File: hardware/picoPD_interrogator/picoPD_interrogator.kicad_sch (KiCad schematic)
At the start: 29 parts, among them Q1 rohm-RE1C002UN, Q2 rohm-RE1C002UN, Q3 rohm-RE1C002UN, Q4 rohm-RE1C002UN, U2 ST-LM393QT

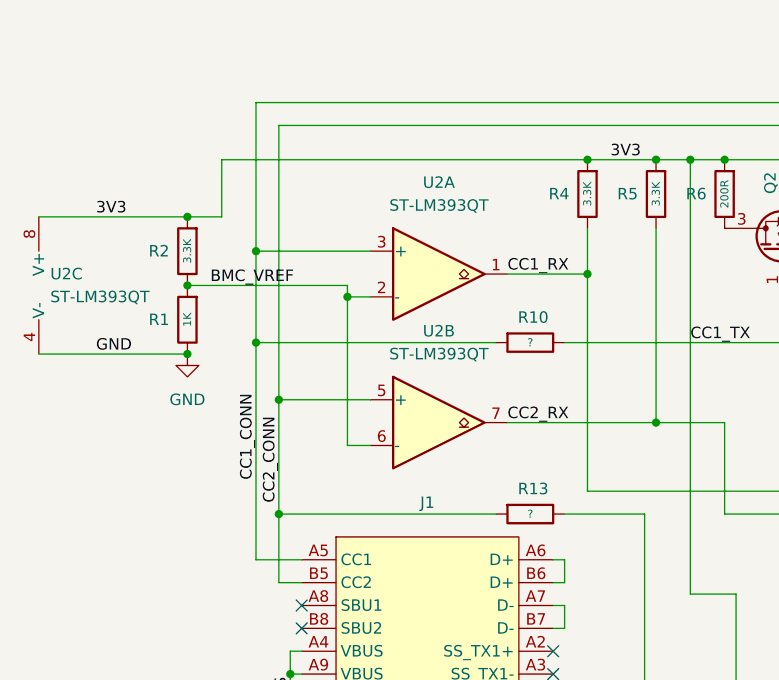
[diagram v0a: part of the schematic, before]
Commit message: Schematic - swapped comparator + and - inputs.
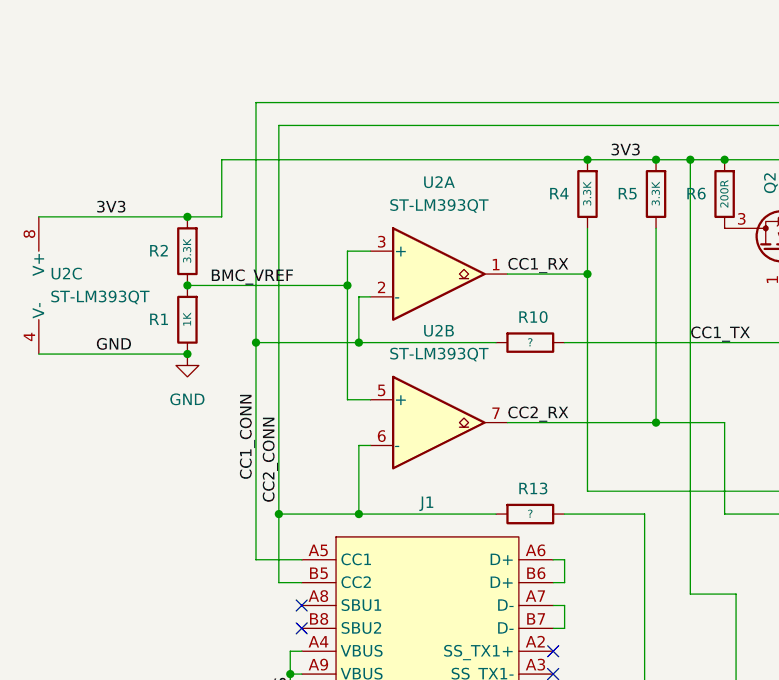
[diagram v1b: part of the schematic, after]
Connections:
- net BMC_VREF: now also U2.3 (+), U2.5 (+); no longer U2.2 (-), U2.6 (-)
- net CC1_CONN: now also U2.2 (-); no longer U2.3 (+)
- net CC2_CONN: now also U2.6 (-); no longer U2.5 (+)
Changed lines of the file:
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@@
+	)
+	(junction
+		(at 74.93 110.49)
+		(diameter 0)
+		(color 0 0 0 0)
+	)
+	(junction
+		(at 74.93 102.87)
+		(diameter 0)
+		(color 0 0 0 0)
+	)
+	(junction
+		(at 220.98 52.07)
+		(diameter 0)
+		(color 0 0 0 0)
+	)
+	(junction
+		(at 115.57 35.56)
+		(diameter 0)
+		(color 0 0 0 0)
+	)
+	(junction
+		(at 73.66 74.93)
+		(diameter 0)
+		(color 0 0 0 0)
+	)
+	(junction
+		(at 135.89 45.72)
+		(diameter 0)
+		(color 0 0 0 0)
+	)
+	(junction
+		(at 170.18 69.85)
+		(diameter 0)
+		(color 0 0 0 0)
 	)
 	(junction
@@
 	)
 	(junction
-		(at 74.93 110.49)
-		(diameter 0)
-		(color 0 0 0 0)
-	)
-	(junction
-		(at 74.93 102.87)
-		(diameter 0)
-		(color 0 0 0 0)
-	)
-	(junction
-		(at 220.98 52.07)
-		(diameter 0)
-		(color 0 0 0 0)
-	)
-	(junction
-		(at 115.57 35.56)
-		(diameter 0)
-		(color 0 0 0 0)
-	)
-	(junction
-		(at 73.66 74.93)
-		(diameter 0)
-		(color 0 0 0 0)
-	)
-	(junction
-		(at 135.89 45.72)
-		(diameter 0)
-		(color 0 0 0 0)
-	)
-	(junction
-		(at 170.18 69.85)
-		(diameter 0)
-		(color 0 0 0 0)
-	)
-	(junction
 		(at 231.14 100.33)
 		(diameter 0)
@@
 	)
 	(junction
-		(at 81.28 50.8)
-		(diameter 0)
-		(color 0 0 0 0)
-	)
-	(junction
 		(at 205.74 69.85)
 		(diameter 0)
@@
 	)
 	(junction
+		(at 81.28 49.53)
+		(diameter 0)
+		(color 0 0 0 0)
+	)
+	(junction
 		(at 205.74 95.25)
 		(diameter 0)
@@
 	)
 	(junction
+		(at 82.55 55.88)
+		(diameter 0)
+		(color 0 0 0 0)
+	)
+	(junction
 		(at 205.74 107.95)
 		(diameter 0)
@@
 	)
 	(junction
-		(at 71.12 45.72)
+		(at 82.55 74.93)
 		(diameter 0)
 		(color 0 0 0 0)
@@
 	)
 	(junction
-		(at 73.66 62.23)
-		(diameter 0)
-		(color 0 0 0 0)
-	)
-	(junction
 		(at 71.12 55.88)
 		(diameter 0)
@@
 	(wire
 		(pts
-			(xy 73.66 62.23) (xy 83.82 62.23)
-		)
-		(stroke
-			(width 0)
-			(type default)
-		)
-	)
-	(wire
-		(pts
 			(xy 170.18 57.15) (xy 172.72 57.15)
 		)
@@
 	(wire
 		(pts
+			(xy 82.55 55.88) (xy 71.12 55.88)
+		)
+		(stroke
+			(width 0)
+			(type default)
+		)
+	)
+	(wire
+		(pts
 			(xy 74.93 92.71) (xy 74.93 90.17)
 		)
@@
 	(wire
 		(pts
-			(xy 97.79 55.88) (xy 71.12 55.88)
+			(xy 97.79 55.88) (xy 82.55 55.88)
 		)
 		(stroke
@@
 	(wire
 		(pts
+			(xy 81.28 62.23) (xy 83.82 62.23)
+		)
+		(stroke
+			(width 0)
+			(type default)
+		)
+	)
+	(wire
+		(pts
 			(xy 123.19 35.56) (xy 208.28 35.56)
 		)
@@
 	(wire
 		(pts
+			(xy 71.12 29.21) (xy 71.12 55.88)
+		)
+		(stroke
+			(width 0)
+			(type default)
+		)
+	)
+	(wire
+		(pts
 			(xy 157.48 140.97) (xy 143.51 140.97)
 		)
@@
 	(wire
 		(pts
-			(xy 81.28 50.8) (xy 83.82 50.8)
-		)
-		(stroke
-			(width 0)
-			(type default)
-		)
-	)
-	(wire
-		(pts
 			(xy 105.41 85.09) (xy 105.41 87.63)
 		)
@@
 	(wire
 		(pts
-			(xy 71.12 29.21) (xy 71.12 45.72)
-		)
-		(stroke
-			(width 0)
-			(type default)
-		)
-	)
-	(wire
-		(pts
 			(xy 187.96 107.95) (xy 187.96 105.41)
 		)
@@
 	(wire
 		(pts
-			(xy 71.12 45.72) (xy 71.12 55.88)
-		)
-		(stroke
-			(width 0)
-			(type default)
-		)
-	)
-	(wire
-		(pts
 			(xy 143.51 140.97) (xy 143.51 116.84)
 		)
@@
 	(wire
 		(pts
-			(xy 73.66 74.93) (xy 73.66 62.23)
+			(xy 82.55 50.8) (xy 82.55 55.88)
 		)
 		(stroke
@@
 	(wire
 		(pts
+			(xy 81.28 49.53) (xy 81.28 45.72)
+		)
+		(stroke
+			(width 0)
+			(type default)
+		)
+	)
+	(wire
+		(pts
 			(xy 105.41 55.88) (xy 133.35 55.88)
 		)
@@
 	(wire
 		(pts
-			(xy 73.66 74.93) (xy 97.79 74.93)
+			(xy 73.66 74.93) (xy 82.55 74.93)
 		)
 		(stroke
@@
 	(wire
 		(pts
+			(xy 83.82 50.8) (xy 82.55 50.8)
+		)
+		(stroke
+			(width 0)
+			(type default)
+		)
+	)
+	(wire
+		(pts
 			(xy 74.93 97.79) (xy 74.93 95.25)
 		)
@@
 	(wire
 		(pts
+			(xy 73.66 31.75) (xy 73.66 74.93)
+		)
+		(stroke
+			(width 0)
+			(type default)
+		)
+	)
+	(wire
+		(pts
 			(xy 168.91 41.91) (xy 218.44 41.91)
 		)
@@
 	(wire
 		(pts
-			(xy 81.28 50.8) (xy 81.28 49.53)
-		)
-		(stroke
-			(width 0)
-			(type default)
-		)
-	)
-	(wire
-		(pts
 			(xy 170.18 82.55) (xy 170.18 69.85)
 		)
@@
 	(wire
 		(pts
-			(xy 83.82 67.31) (xy 81.28 67.31)
-		)
-		(stroke
-			(width 0)
-			(type default)
-		)
-	)
-	(wire
-		(pts
-			(xy 71.12 45.72) (xy 83.82 45.72)
-		)
-		(stroke
-			(width 0)
-			(type default)
-		)
-	)
-	(wire
-		(pts
 			(xy 105.41 87.63) (xy 104.14 87.63)
 		)
@@
 	(wire
 		(pts
+			(xy 81.28 45.72) (xy 83.82 45.72)
+		)
+		(stroke
+			(width 0)
+			(type default)
+		)
+	)
+	(wire
+		(pts
+			(xy 82.55 74.93) (xy 97.79 74.93)
+		)
+		(stroke
+			(width 0)
+			(type default)
+		)
+	)
+	(wire
+		(pts
 			(xy 142.24 85.09) (xy 172.72 85.09)
 		)
@@
 	(wire
 		(pts
+			(xy 63.5 49.53) (xy 81.28 49.53)
+		)
+		(stroke
+			(width 0)
+			(type default)
+		)
+	)
+	(wire
+		(pts
+			(xy 82.55 67.31) (xy 82.55 74.93)
+		)
+		(stroke
+			(width 0)
+			(type default)
+		)
+	)
+	(wire
+		(pts
 			(xy 170.18 82.55) (xy 172.72 82.55)
 		)
@@
 	(wire
 		(pts
-			(xy 81.28 67.31) (xy 81.28 50.8)
-		)
-		(stroke
-			(width 0)
-			(type default)
-		)
-	)
-	(wire
-		(pts
 			(xy 99.06 64.77) (xy 115.57 64.77)
 		)
@@
 	(wire
 		(pts
-			(xy 73.66 62.23) (xy 73.66 31.75)
-		)
-		(stroke
-			(width 0)
-			(type default)
-		)
-	)
-	(wire
-		(pts
 			(xy 190.5 118.11) (xy 190.5 105.41)
 		)
@@
 	(wire
 		(pts
-			(xy 63.5 49.53) (xy 81.28 49.53)
-		)
-		(stroke
-			(width 0)
-			(type default)
-		)
-	)
-	(wire
-		(pts
 			(xy 203.2 62.23) (xy 208.28 62.23)
 		)
@@
 		)
 		(stroke
+			(width 0)
+			(type default)
+		)
+	)
+	(wire
+		(pts
+			(xy 81.28 49.53) (xy 81.28 62.23)
+		)
+		(stroke
+			(width 0)
+			(type default)
+		)
+	)
+	(wire
+		(pts
+			(xy 82.55 67.31) (xy 83.82 67.31)
+		)
+		(stroke

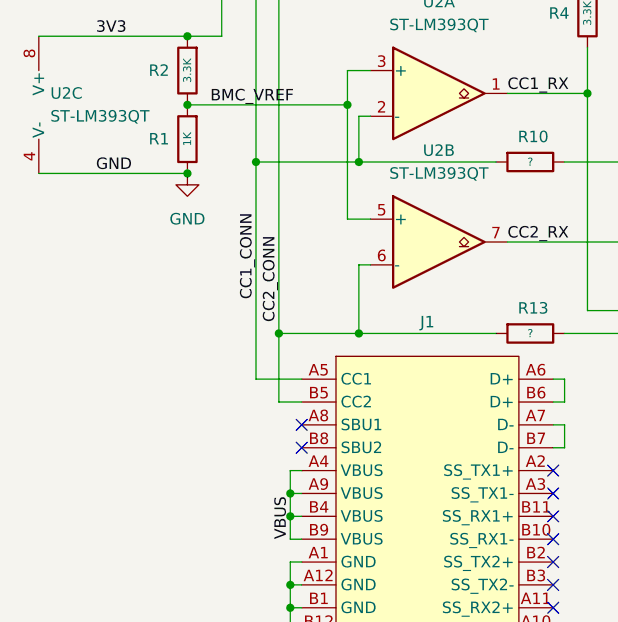
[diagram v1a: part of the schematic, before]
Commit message: Schematic - Added Rd pulldown resistors.
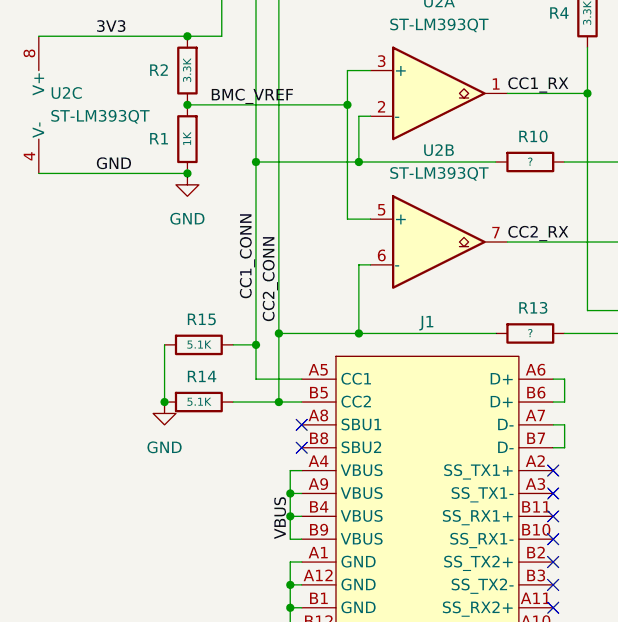
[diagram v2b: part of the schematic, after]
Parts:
- added R14, R15: 5.1K, Resistor_SMD:R_0201_0603Metric, symbol Device:R
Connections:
- net CC1_CONN: now also R15.1
- net CC2_CONN: now also R14.1
- net GND: now also R14.2, R15.2

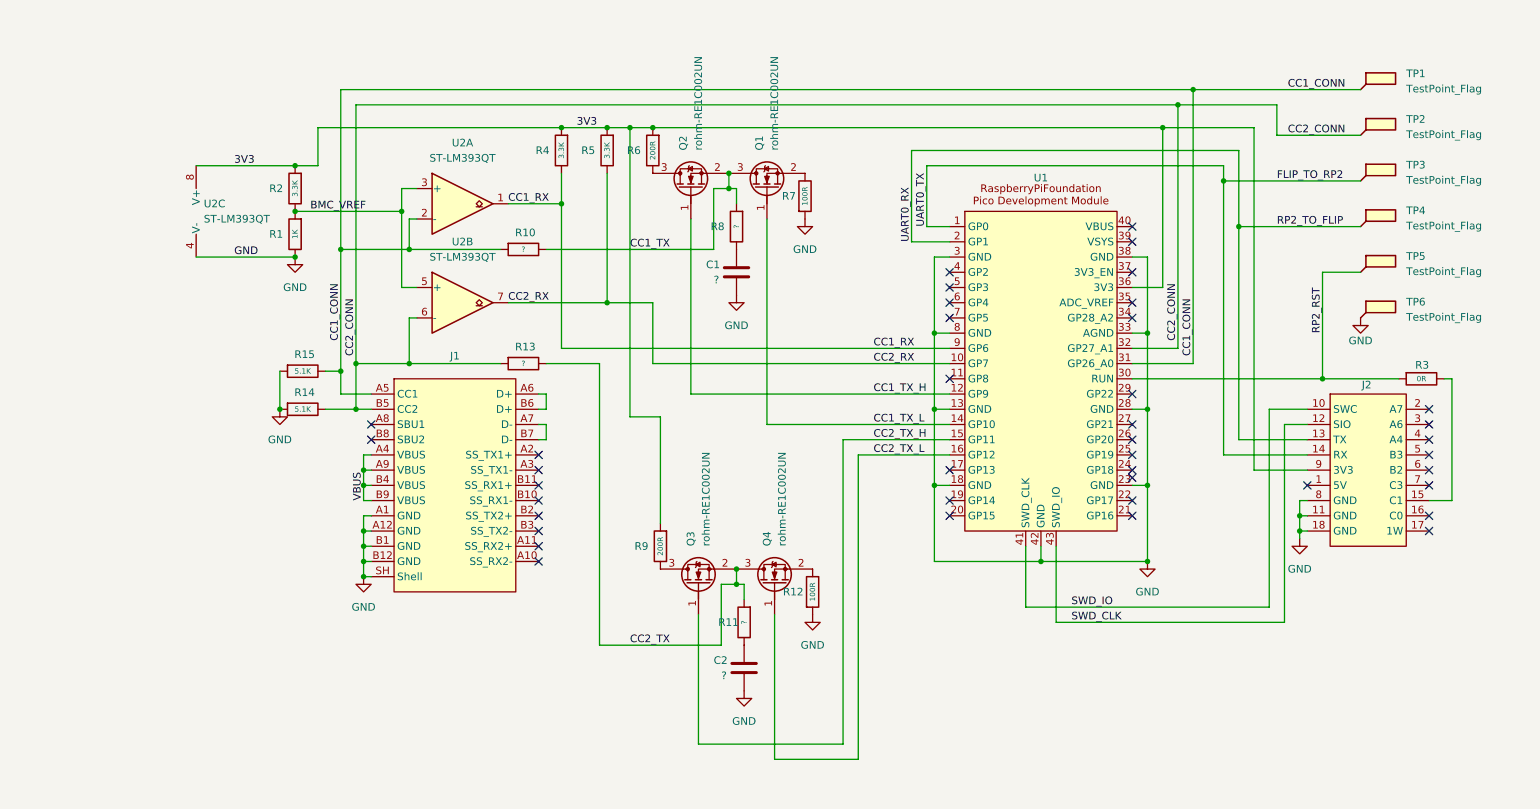
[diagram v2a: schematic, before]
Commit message: Seperated out RPI Pico MCU module on schematic.
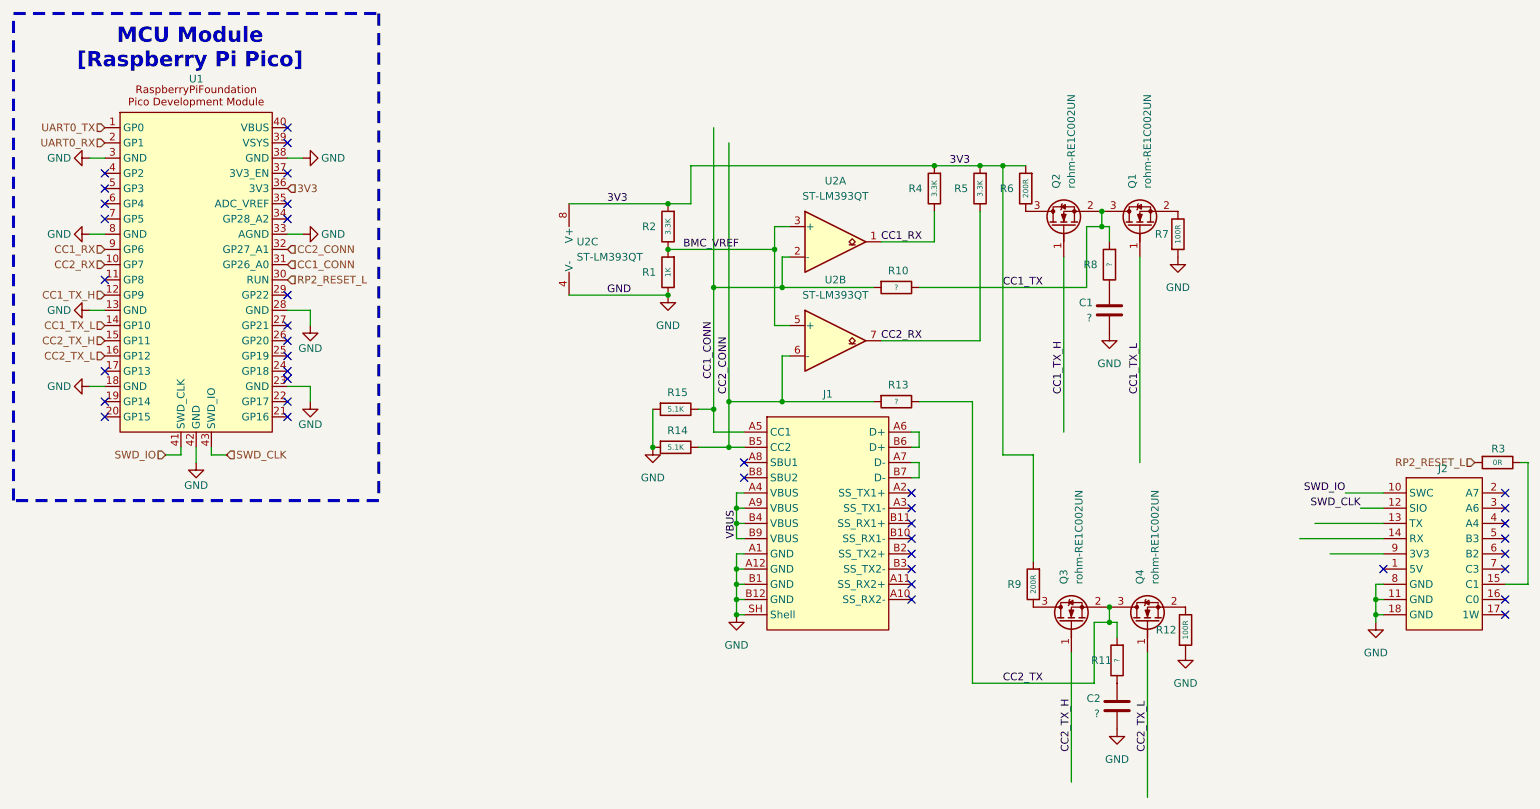
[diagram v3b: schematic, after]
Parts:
- removed TP1, TP2, TP3, TP4, TP5, TP6: TestPoint_Flag, picoPD_interrogator:Harwin_S2751, symbol Connector:TestPoint_Flag
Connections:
- net 3V3: no longer J2.9 (3V3)
- net FLIP_TO_RP2: no longer names the net of J2.14 (RX)
- net FLIP_TO_RP2: no longer U1.1 (GP0)
- net RP2_RST renamed RP2_RESET_L
- net RP2_TO_FLIP: no longer names the net of J2.13 (TX)
- net RP2_TO_FLIP: no longer U1.2 (GP1)
- new net UART0_RX: U1.2 (GP1)
- new net UART0_TX: U1.1 (GP0)
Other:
- note added: "MCU Module [Raspberry Pi Pico]"
- moved on the sheet: C1, C2, J1, J2, Q1, Q2, Q3, Q4, R1, R10, R11, R12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

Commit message: Cleaned up schematic layout.
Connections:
- net 3V3: now also J2.9 (3V3), R4.1; no longer Q1.3 (D), Q2.2 (S), R10.1, R4.2, R8.2
- net CC1_CONN: now also R15.2; no longer R15.1
- net CC1_RX: now also R4.2; no longer R4.1
- net CC2_CONN: now also R13.1, R14.2; no longer R13.2, R14.1
- net CC2_TX: now also R13.2; no longer R13.1
- net GND: now also R14.1, R15.1; no longer R14.2, R15.2
- net UART0_RX: now also J2.13 (TX)
- net UART0_TX: now also J2.14 (RX)
- new net CC1_TX: Q1.3 (D), Q2.2 (S), R10.1, R8.2
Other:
- note added: "CC pull-down resistors"
- note added: "Flipper Zero Interconnect"
- note added: "Interrogation port 0 [GS8 USB-C receptacle]"
- note added: "USB-PD [Receive]"
- note added: "USB-PD [Transmit]"
- moved on the sheet: C1, C2, J1, J2, Q1, Q2, Q3, Q4, R1, R10, R11, R12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
